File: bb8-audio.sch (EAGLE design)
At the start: 27 parts, among them IC1 7805L, IC3 74LS125N

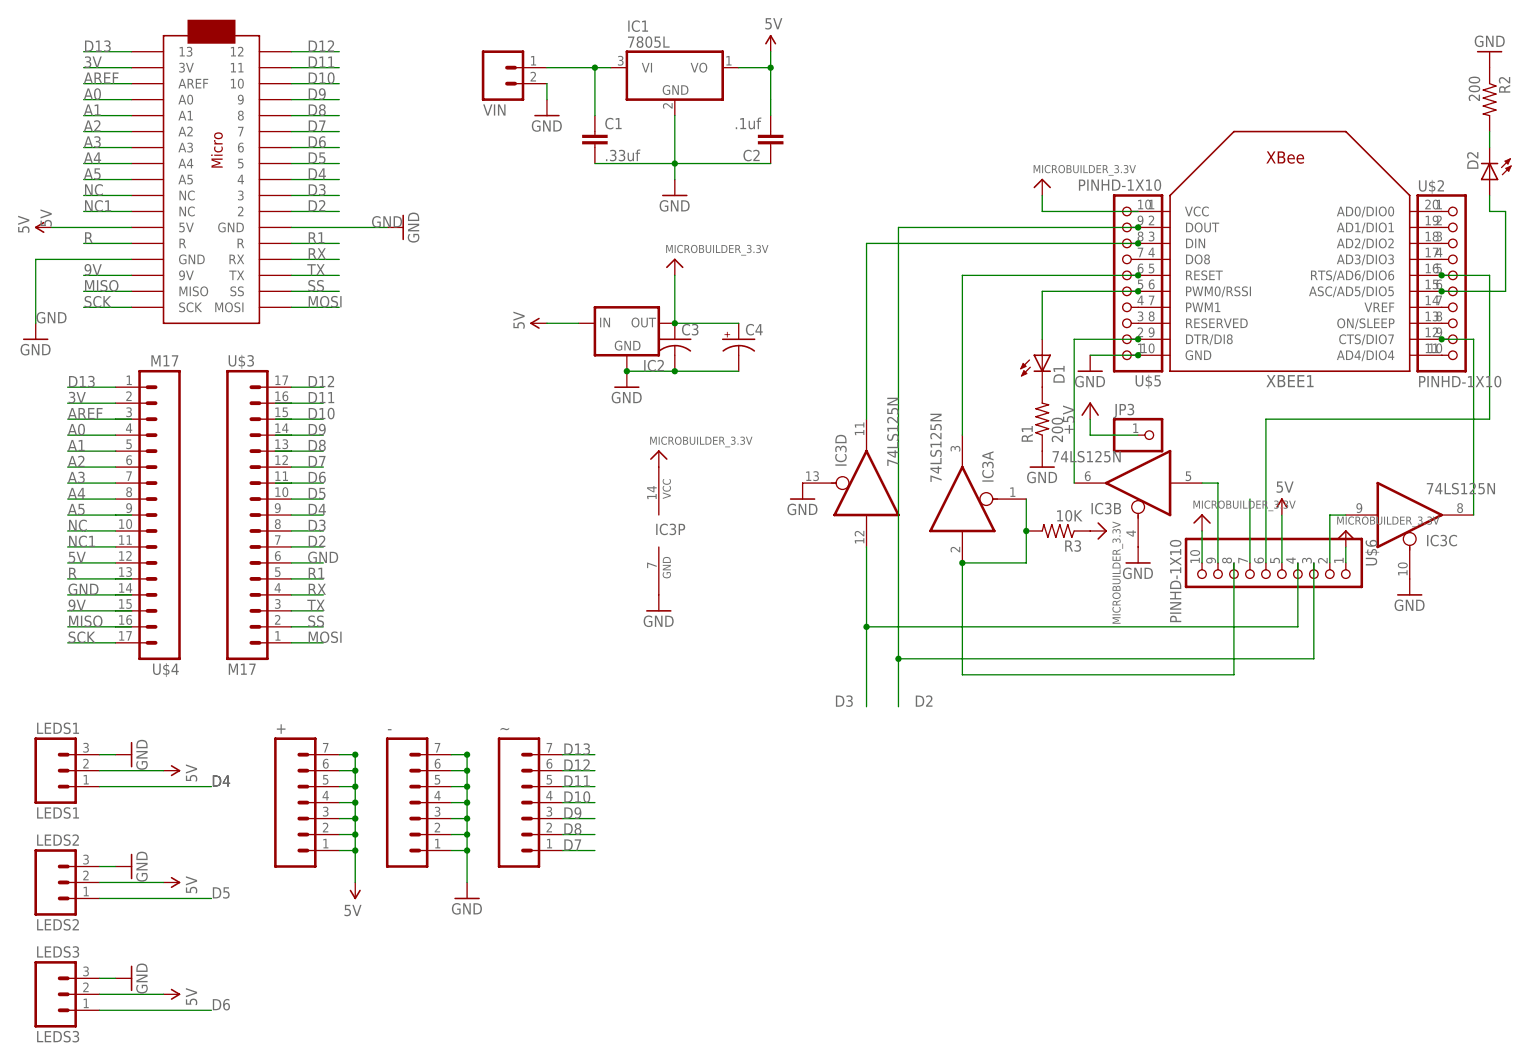
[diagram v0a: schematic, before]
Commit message: Updated to use Arduino Pro Mini
Updated board and schematic to have an arduino pro mini instead of a
micro.
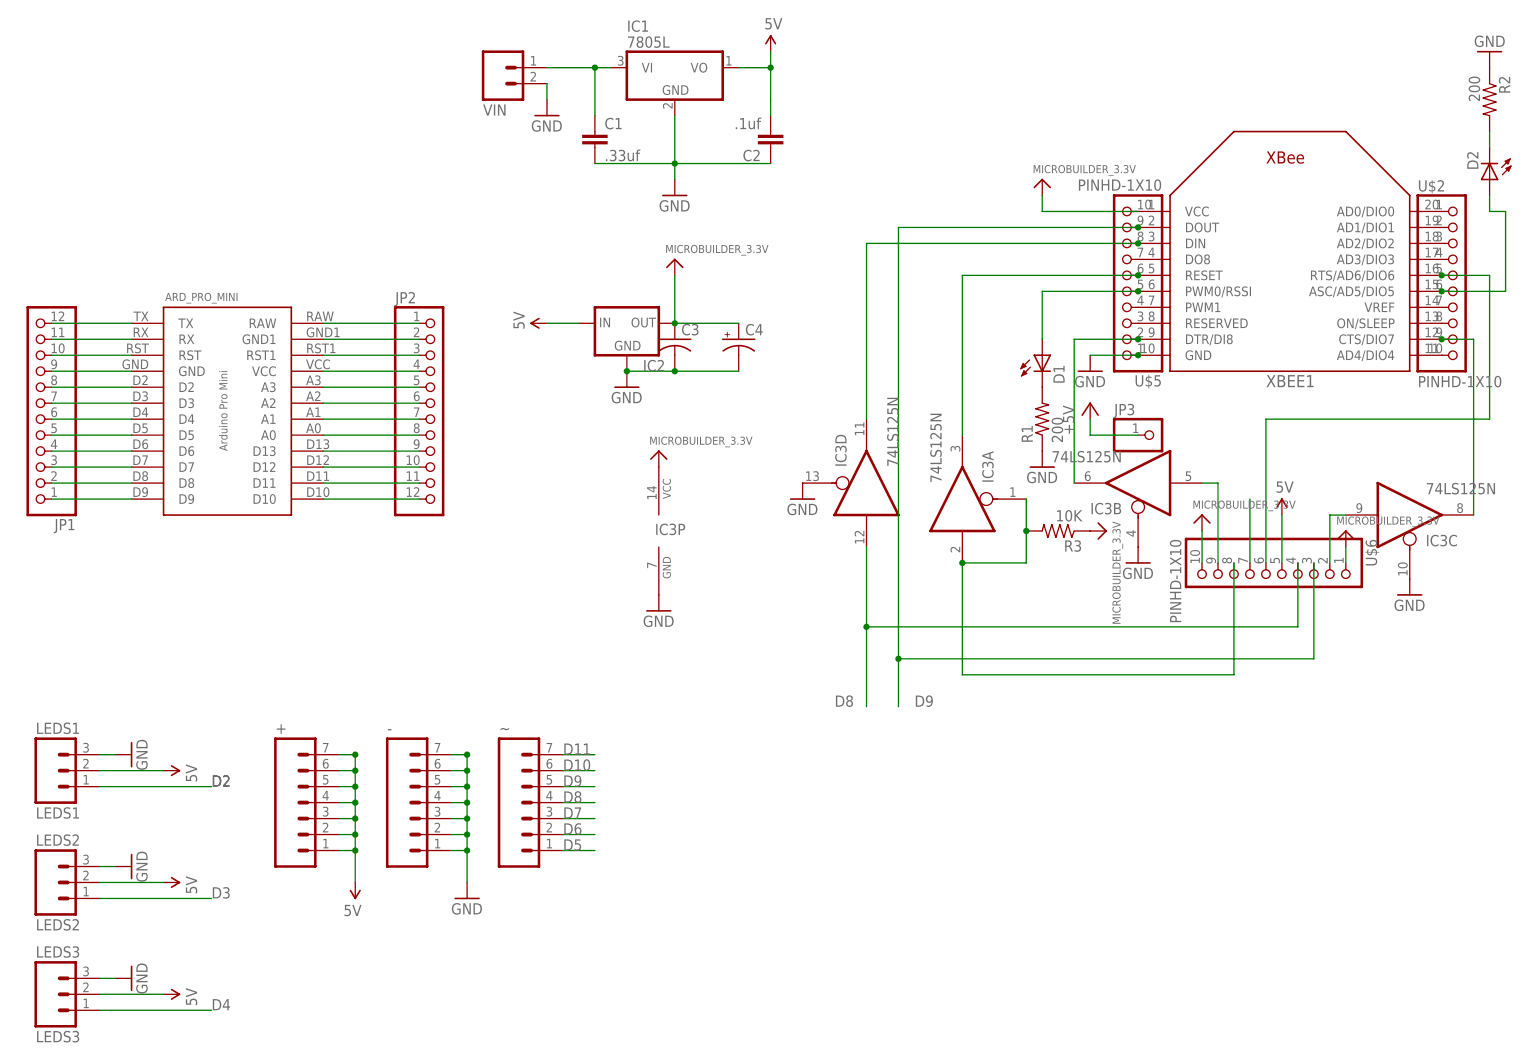
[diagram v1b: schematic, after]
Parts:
- removed U$1: ARDUINOMICRO, adafruit:ARDUINOMICRO
- removed U$3, U$4: M17, SparkFun-Connectors:M17
- added ARD_PRO_MINI: ARD_PRO_MINI, Arduino-Pro-Mini:ARD_PRO_MINI
- added JP1, JP2: (no value), adafruit:PINHD-1X12-CB
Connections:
- removed net 3V: U$1.3V, U$4.2
- removed net 9V: U$1.9V, U$4.15
- removed net A4: U$1.A4, U$4.8
- removed net A5: U$1.A5, U$4.9
- removed net AREF: U$1.AREF, U$4.3
- removed net MISO: U$1.MISO, U$4.16
- removed net MOSI: U$1.MOSI, U$3.1
- removed net NC: U$1.NC@2, U$4.10
- removed net NC1: U$1.NC@1, U$4.11
- removed net R: U$1.R@1, U$4.13
- removed net R1: U$1.R@2, U$3.5
- removed net SCK: U$1.SCK, U$4.17
- removed net SS: U$1.SS, U$3.2
- new net RAW: ARD_PRO_MINI.RAW, JP2.1
- new net RST: ARD_PRO_MINI.RST, ARD_PRO_MINI.RST1, JP1.10, JP2.3
- new net VCC: ARD_PRO_MINI.VCC, JP2.4
- net 5V: no longer U$1.5V, U$4.12
- net A0: now also ARD_PRO_MINI.A0, JP2.8; no longer U$1.A0, U$4.4
- net A1: now also ARD_PRO_MINI.A1, JP2.7; no longer U$1.A1, U$4.5
- net A2: now also ARD_PRO_MINI.A2, JP2.6; no longer U$1.A2, U$4.6
- net A3: now also ARD_PRO_MINI.A3, JP2.5; no longer U$1.A3, U$4.7
- net D10: now also ARD_PRO_MINI.D10, JP2.12, ~.6; no longer U$1.10, U$3.15, ~.4
- net D11: now also ARD_PRO_MINI.D11, JP2.11, ~.7; no longer U$1.11, U$3.16, ~.5
- net D12: now also ARD_PRO_MINI.D12, JP2.10; no longer U$1.12, U$3.17, ~.6
- net D13: now also ARD_PRO_MINI.D13, JP2.9; no longer U$1.13, U$4.1, ~.7
- net D2: now also ARD_PRO_MINI.D2, JP1.8, LEDS1.1; no longer U$1.2, U$3.7, U$5.9, U$6.3, XBEE1.DOUT
- net D3: now also ARD_PRO_MINI.D3, JP1.7, LEDS2.1; no longer IC3D.I, U$1.3, U$3.8, U$6.4
- net D4: now also ARD_PRO_MINI.D4, JP1.6, LEDS3.1; no longer LEDS1.1, U$1.4, U$3.9
- net D5: now also ARD_PRO_MINI.D5, JP1.5, ~.1; no longer LEDS2.1, U$1.5, U$3.10
- net D6: now also ARD_PRO_MINI.D6, JP1.4, ~.2; no longer LEDS3.1, U$1.6, U$3.11
- net D7: now also ARD_PRO_MINI.D7, JP1.3, ~.3; no longer U$1.7, U$3.12, ~.1
- net D8: now also ARD_PRO_MINI.D8, IC3D.I, JP1.2, U$6.4, ~.4; no longer U$1.8, U$3.13, ~.2
- net D9: now also ARD_PRO_MINI.D9, JP1.1, U$5.9, U$6.3, XBEE1.DOUT, ~.5; no longer U$1.9, U$3.14, ~.3
- net GND: now also ARD_PRO_MINI.GND, ARD_PRO_MINI.GND1, JP1.9, JP2.2; no longer U$1.GND, U$1.GND@1, U$3.6, U$4.14
- net RX: now also ARD_PRO_MINI.RX, JP1.11; no longer U$1.RX, U$3.4
- net TX: now also ARD_PRO_MINI.TX, JP1.12; no longer U$1.TX, U$3.3
